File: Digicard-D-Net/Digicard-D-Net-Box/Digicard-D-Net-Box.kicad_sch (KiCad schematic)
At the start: 9 parts, among them J1 6P4C, J2 6P4C, J3 DE9_Male, T1 1:1

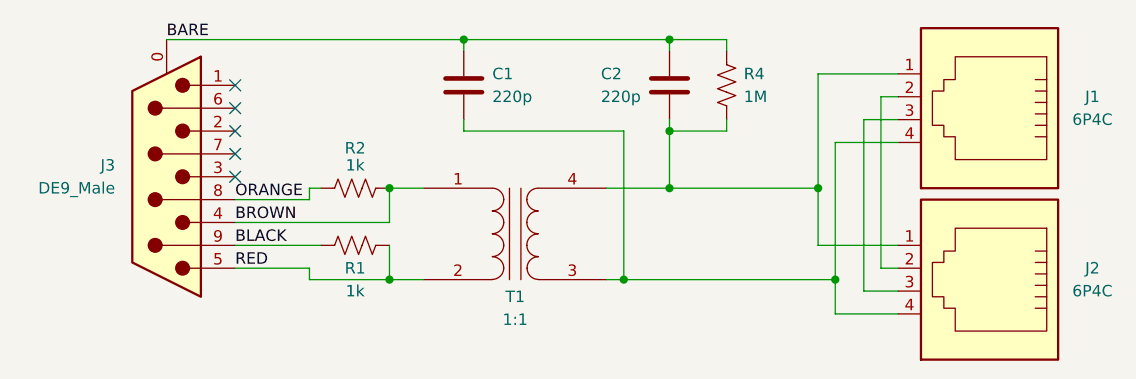
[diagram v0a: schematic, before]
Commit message: Update the Digicard projects to kicad8 and use the shared symbol library
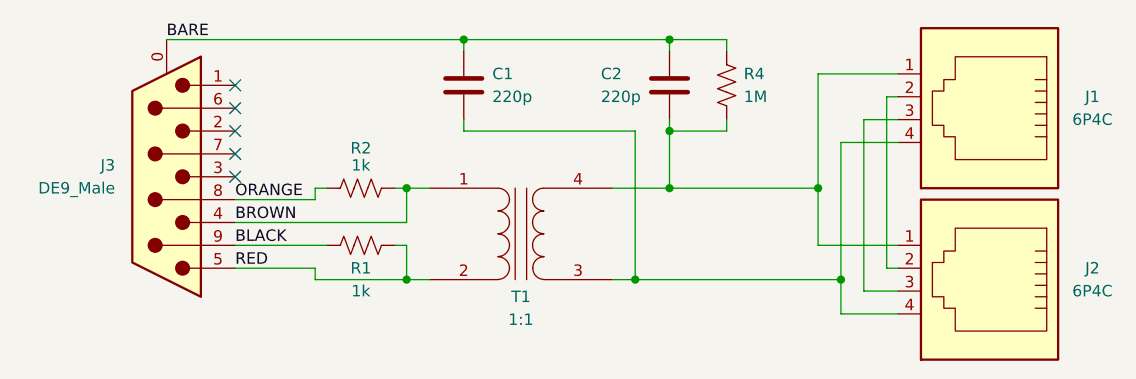
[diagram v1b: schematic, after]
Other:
- moved on the sheet: R1, R2, T1
